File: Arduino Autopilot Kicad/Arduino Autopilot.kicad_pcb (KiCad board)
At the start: 2 copper layers, 100 x 77 mm, 28 parts, among them J1 12V_in, J2 to_clock, J3 to_RTC, J4 to_LCD, SW1 SW_Push

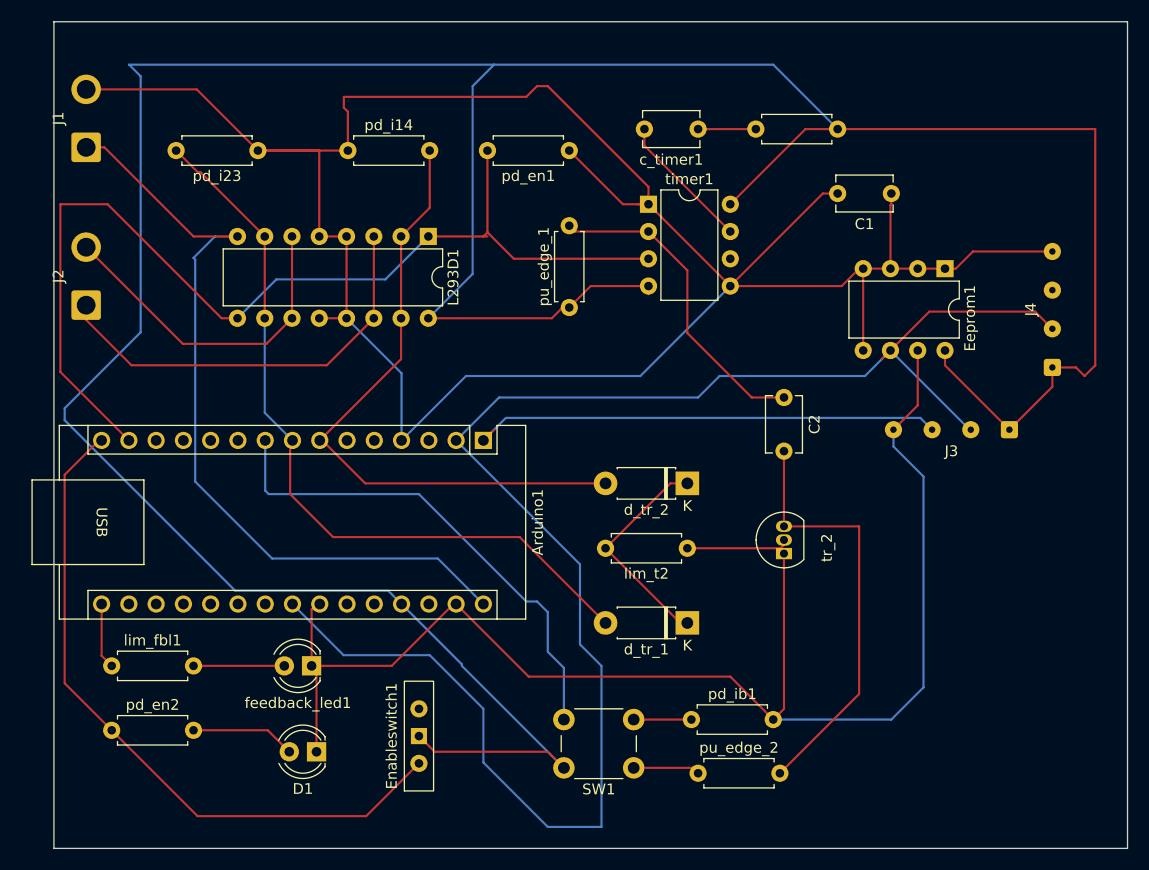
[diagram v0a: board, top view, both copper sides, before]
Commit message: updated board circuit, added serial commands parsing, update documentation
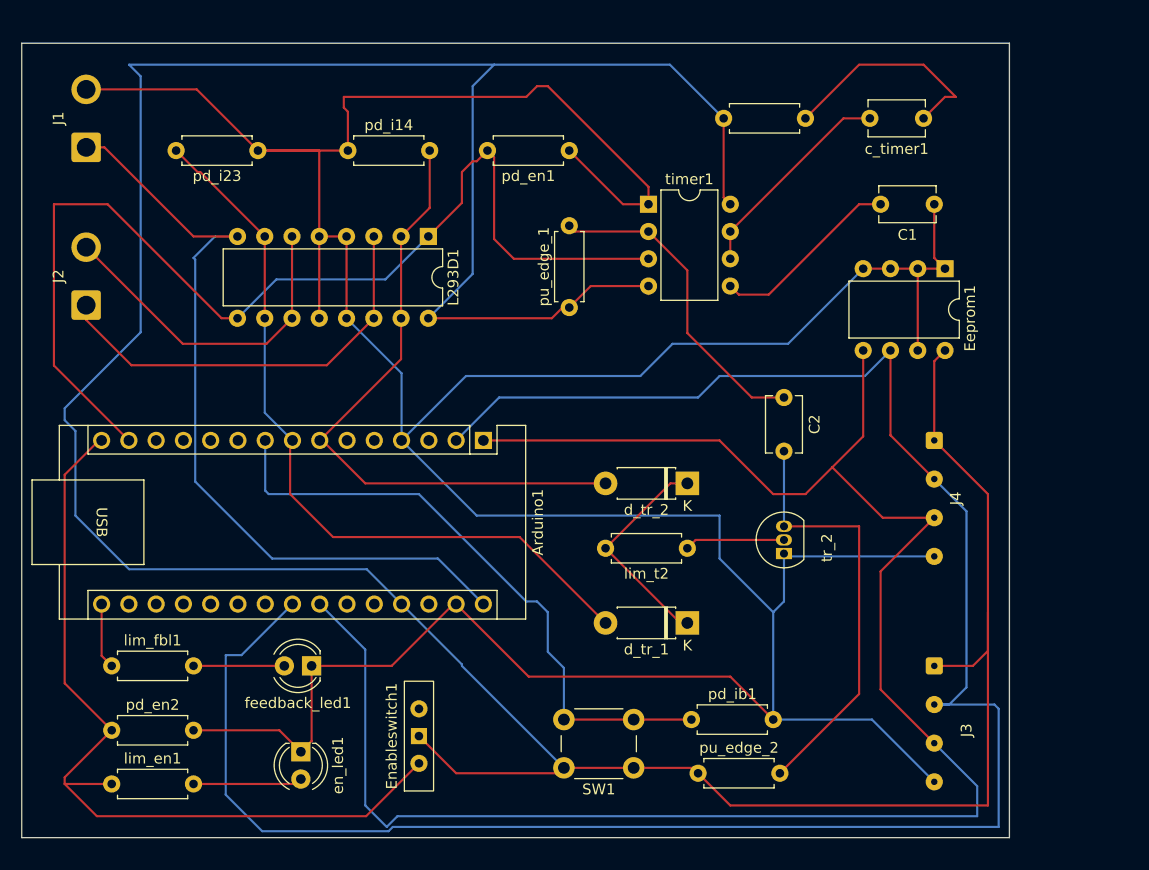
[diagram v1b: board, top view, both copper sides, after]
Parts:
- removed D1: LED, LED_THT:LED_D4.0mm
- added en_led1: LED, LED_THT:LED_D4.0mm, F.Cu at (55.0, 116.0)
- added lim_en1: R, Resistor_THT:R_Axial_DIN0207_L6.3mm_D2.5mm_P7.62mm_Horizontal, F.Cu at (37.4, 119.0)
- moved J3 23.1 mm to (114.0, 108.0), turned to -90 degrees
- moved c_timer1 21.0 mm to (113.0, 57.0)
- moved J4 12.9 mm to (114.0, 87.0), turned to -90 degrees
- moved r_timer1 4.73 mm to (102.0, 57.0), turned to 180 degrees
- moved C1 4.12 mm to (114.0, 65.0)
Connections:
- Arduino1 pad 1: Net-(Arduino1-D1/TX) -> Net-(Arduino1-A5)
- Arduino1 pad 24: GND -> Net-(Arduino1-A5)
- Eeprom1 pad 5: GND -> Net-(Arduino1-A5)
- J3 pad 3: Net-(Arduino1-D1/TX) -> Net-(Arduino1-A5)
- J4 pad 3: GND -> Net-(Arduino1-A5)
- pd_en2 pad 2: Net-(D1-A) -> GND
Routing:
- net Net-(Arduino1-A5): track 0.00 -> 171.5 mm
- net Net-(Arduino1-D1/TX): track 44.5 -> 0.00 mm
- net Net-(Arduino1-A4): track 154.8 -> 193.8 mm
- net Net-(c_timer1-Pad1): track 5.38 -> 21.1 mm
- net GND: track 340.4 -> 354.9 mm
- net Net-(Arduino1-D12): track 64.5 -> 78.0 mm
- net Net-(en_led1-A): track 0.00 -> 10.2 mm
- net +5V: track 315.5 -> 325.6 mm
- net Net-(D1-A): track 9.75 -> 0.00 mm
- net Net-(timer1-DIS): track 12.9 -> 19.9 mm
- net Net-(Arduino1-D6): track 51.7 -> 58.2 mm
- net Net-(Arduino1-D11): track 96.9 -> 102.2 mm
- net Net-(timer1-CV): track 13.0 -> 17.8 mm
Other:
- board size 100 x 77 mm -> 92 x 74 mm

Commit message: fixed dst management when sending manual inputs, fixed delay capacitor wiring in circuit
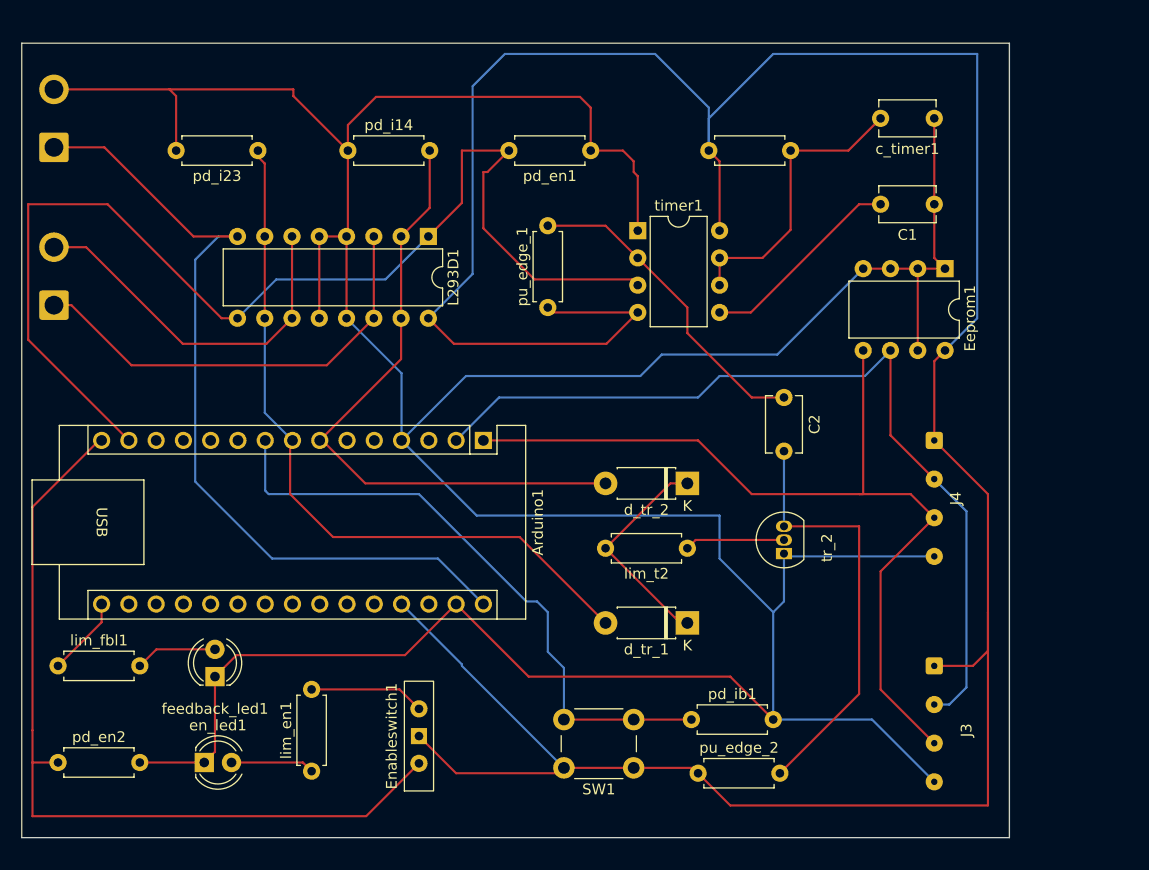
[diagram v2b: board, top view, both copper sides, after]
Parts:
- moved lim_en1 18.7 mm to (56.0, 117.8), turned to 90 degrees
- moved en_led1 9.06 mm to (46.0, 117.0), turned to 0 degrees
- moved feedback_led1 9.06 mm to (47.0, 109.0), turned to 90 degrees
- moved pd_en2 5.83 mm to (32.4, 117.0)
- moved lim_fbl1 5.00 mm to (32.4, 108.0)
- moved r_timer1 3.30 mm to (100.6, 60.0)
- moved J1 3.00 mm to (32.0, 59.7)
- moved J2 3.00 mm to (32.0, 74.4)
- moved timer1 2.66 mm to (86.4, 67.5)
- moved pd_en1 2.00 mm to (82.0, 60.0)
- moved pu_edge_1 2.00 mm to (78.0, 74.6)
- moved c_timer1 1.00 mm to (114.0, 57.0)
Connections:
- Arduino1 pad 1: Net-(Arduino1-A5) -> Net-(Arduino1-D1/TX)
- Arduino1 pad 2: Net-(Arduino1-A4) -> Net-(Arduino1-D0/RX)
- Arduino1 pad 23: Net-(Arduino1-A4) -> unconnected-(Arduino1-A4-Pad23)
- Arduino1 pad 24: Net-(Arduino1-A5) -> unconnected-(Arduino1-A5-Pad24)
- Eeprom1 pad 5: Net-(Arduino1-A5) -> Net-(Arduino1-D1/TX)
- Eeprom1 pad 6: Net-(Arduino1-A4) -> Net-(Arduino1-D0/RX)
- Enableswitch1 pad 3: unconnected-(Enableswitch1-A-Pad3) -> Net-(Enableswitch1-A)
- J3 pad 2: Net-(Arduino1-A4) -> Net-(Arduino1-D0/RX)
- J3 pad 3: Net-(Arduino1-A5) -> Net-(Arduino1-D1/TX)
- J4 pad 2: Net-(Arduino1-A4) -> Net-(Arduino1-D0/RX)
- J4 pad 3: Net-(Arduino1-A5) -> Net-(Arduino1-D1/TX)
- c_timer1 pad 1: Net-(c_timer1-Pad1) -> GND
- lim_en1 pad 1: Net-(Arduino1-D12) -> Net-(en_led1-A)
- lim_en1 pad 2: Net-(en_led1-A) -> Net-(Enableswitch1-A)
- pd_i23 pad 1: GND -> Net-(Arduino1-D5)
- pd_i23 pad 2: Net-(Arduino1-D5) -> GND
- r_timer1 pad 1: Net-(c_timer1-Pad1) -> Net-(timer1-DIS)
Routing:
- net Net-(Arduino1-A4): track 193.8 -> 0.00 mm
- net Net-(Arduino1-A5): track 171.5 -> 0.00 mm
- net Net-(Arduino1-D1/TX): track 0.00 -> 83.5 mm
- net Net-(Arduino1-D0/RX): track 0.00 -> 82.4 mm
- net +5V: track 325.6 -> 281.8 mm
- net Net-(c_timer1-Pad1): track 21.1 -> 0.00 mm
- net Net-(Enableswitch1-A): track 0.00 -> 10.7 mm
- net Net-(timer1-DIS): track 19.9 -> 27.2 mm
- net Net-(Arduino1-D11): track 102.2 -> 109.4 mm
- net GND: track 354.9 -> 361.4 mm
- net Net-(Arduino1-D5): track 71.3 -> 67.8 mm
- net Net-(J2-Pin_2): track 31.5 -> 34.5 mm
- net Net-(en_led1-A): track 10.2 -> 7.80 mm
- net Net-(J2-Pin_1): track 39.4 -> 41.5 mm
- net +12C: track 75.9 -> 77.6 mm
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
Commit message: updated pin layout, updated circuit and board design
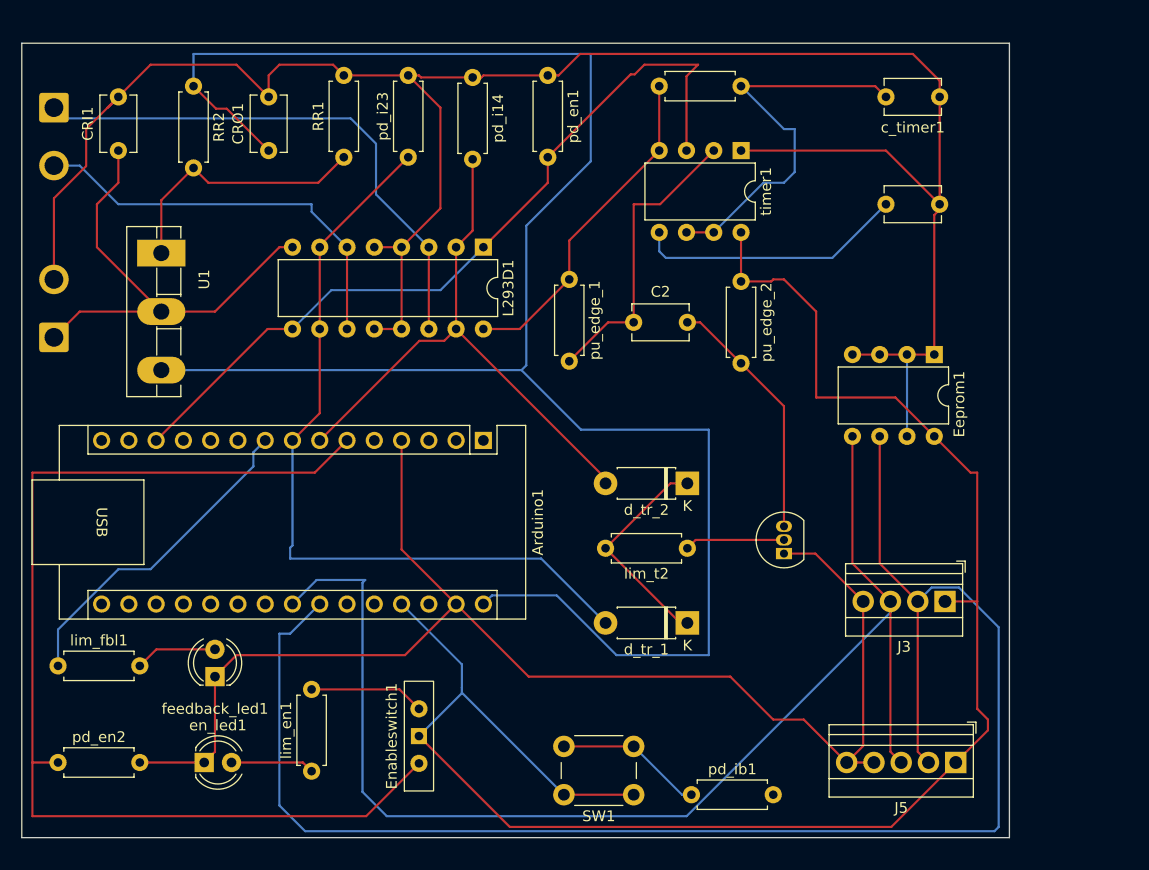
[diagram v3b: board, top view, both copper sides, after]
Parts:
- removed J4: to_LCD, Connector_Wire:SolderWire-0.1sqmm_1x04_P3.6mm_D0.4mm_OD1mm
- added CRI1: 0.1uf, Capacitor_THT:C_Disc_D5.1mm_W3.2mm_P5.00mm, F.Cu at (38.0, 60.0)
- added CRO1: 10uF, Capacitor_THT:C_Disc_D5.1mm_W3.2mm_P5.00mm, F.Cu at (52.0, 60.0)
- added J5: to_RTC, TerminalBlock:TerminalBlock_Xinya_XY308-2.54-5P_1x05_P2.54mm_Horizontal, F.Cu at (116.0, 117.0)
- added RR1: 1k, Resistor_THT:R_Axial_DIN0207_L6.3mm_D2.5mm_P7.62mm_Horizontal, F.Cu at (59.0, 60.6)
- added RR2: 330, Resistor_THT:R_Axial_DIN0207_L6.3mm_D2.5mm_P7.62mm_Horizontal, F.Cu at (45.0, 54.0)
- added U1: LM350_TO3, Package_TO_SOT_THT:TO-3PB-3_Vertical, F.Cu at (42.0, 69.5)
- J3: value to_RTC -> to_LCD; footprint Connector_Wire:SolderWire-0.1sqmm_1x04_P3.6mm_D0.4mm_OD1mm -> TerminalBlock:TerminalBlock_Xinya_XY308-2.54-4P_1x04_P2.54mm_Horizontal
- moved pu_edge_2 46.0 mm to (96.0, 72.2), turned to -90 degrees
- moved J2 18.4 mm to (32.0, 56.0), turned to -90 degrees
- moved J1 17.7 mm to (32.0, 77.4)
- moved C2 15.7 mm to (86.0, 76.0), turned to 0 degrees
- moved pd_i23 14.0 mm to (65.0, 60.6), turned to 90 degrees
- moved pd_i14 13.5 mm to (71.0, 53.2), turned to -90 degrees
- moved timer1 12.2 mm to (96.0, 60.0), turned to -90 degrees
- moved Eeprom1 8.06 mm to (114.0, 79.0)
- moved pd_en1 8.06 mm to (78.0, 53.0), turned to -90 degrees
- moved r_timer1 7.57 mm to (96.0, 54.0)
- moved pd_ib1 7.00 mm to (91.4, 120.0)
- moved J3 6.08 mm to (115.0, 102.0), turned to 180 degrees
- moved L293D1 5.22 mm to (72.0, 69.0)
- moved pu_edge_1 3.30 mm to (80.0, 72.0), turned to -90 degrees
- moved SW1 2.50 mm to (86.0, 120.0)
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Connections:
- Arduino1 pad 1: Net-(Arduino1-D1/TX) -> unconnected-(Arduino1-D1/TX-Pad1)
- Arduino1 pad 13: unconnected-(Arduino1-D10-Pad13) -> Net-(Arduino1-D10)
- Arduino1 pad 14: Net-(Arduino1-D11) -> unconnected-(Arduino1-D11-Pad14)
- Arduino1 pad 15: Net-(Arduino1-D12) -> unconnected-(Arduino1-D12-Pad15)
- Arduino1 pad 16: Net-(Arduino1-D13) -> unconnected-(Arduino1-D13-Pad16)
- Arduino1 pad 2: Net-(Arduino1-D0/RX) -> unconnected-(Arduino1-D0/RX-Pad2)
- Arduino1 pad 23: unconnected-(Arduino1-A4-Pad23) -> Net-(Arduino1-A4)
- Arduino1 pad 24: unconnected-(Arduino1-A5-Pad24) -> Net-(Arduino1-A5)
- Arduino1 pad 30: +12C -> Net-(Arduino1-VIN)
- Arduino1 pad 6: unconnected-(Arduino1-D3-Pad6) -> Net-(Arduino1-D3)
- Eeprom1 pad 5: Net-(Arduino1-D1/TX) -> Net-(Arduino1-A4)
- Eeprom1 pad 6: Net-(Arduino1-D0/RX) -> Net-(Arduino1-A5)
- Enableswitch1 pad 2: Net-(Arduino1-D12) -> Net-(Arduino1-D3)
- J3 pad 2: Net-(Arduino1-D0/RX) -> Net-(Arduino1-A5)
- J3 pad 3: Net-(Arduino1-D1/TX) -> Net-(Arduino1-A4)
- L293D1 pad 1: Net-(Arduino1-D11) -> Net-(Arduino1-D10)
- L293D1 pad 9: Net-(Arduino1-D11) -> Net-(Arduino1-D10)
- SW1 pad 2: Net-(Arduino1-D6) -> Net-(SW1-Pad2)
- lim_fbl1 pad 1: Net-(Arduino1-D13) -> Net-(Arduino1-D6)
- pd_en1 pad 2: Net-(Arduino1-D11) -> Net-(Arduino1-D10)
- pd_en2 pad 1: Net-(Arduino1-D12) -> Net-(Arduino1-D3)
- pd_ib1 pad 1: Net-(Arduino1-D6) -> Net-(SW1-Pad2)
- timer1 pad 3: Net-(Arduino1-D11) -> Net-(Arduino1-D10)
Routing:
- net Net-(Arduino1-VIN): track 0.00 -> 180.1 mm
- net Net-(Arduino1-A5): track 0.00 -> 149.5 mm
- net Net-(Arduino1-A4): track 0.00 -> 118.8 mm
- net Net-(Arduino1-D11): track 109.4 -> 0.00 mm
- net Net-(Arduino1-D3): track 0.00 -> 103.0 mm
- net +5V: track 281.8 -> 194.5 mm
- net Net-(Arduino1-D1/TX): track 83.5 -> 0.00 mm
- net Net-(Arduino1-D0/RX): track 82.4 -> 0.00 mm
- net Net-(Arduino1-D12): track 78.3 -> 0.00 mm
- net Net-(Arduino1-D10): track 0.00 -> 74.8 mm
- net GND: track 361.4 -> 326.4 mm
- net +12C: track 77.6 -> 44.0 mm
- net Net-(Arduino1-D6): track 58.2 -> 30.8 mm
- net Net-(U1-ADJ): track 0.00 -> 24.7 mm
- net Net-(tr_2-C): track 40.1 -> 23.4 mm
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
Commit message: fixed sleep mode, updated diagrams
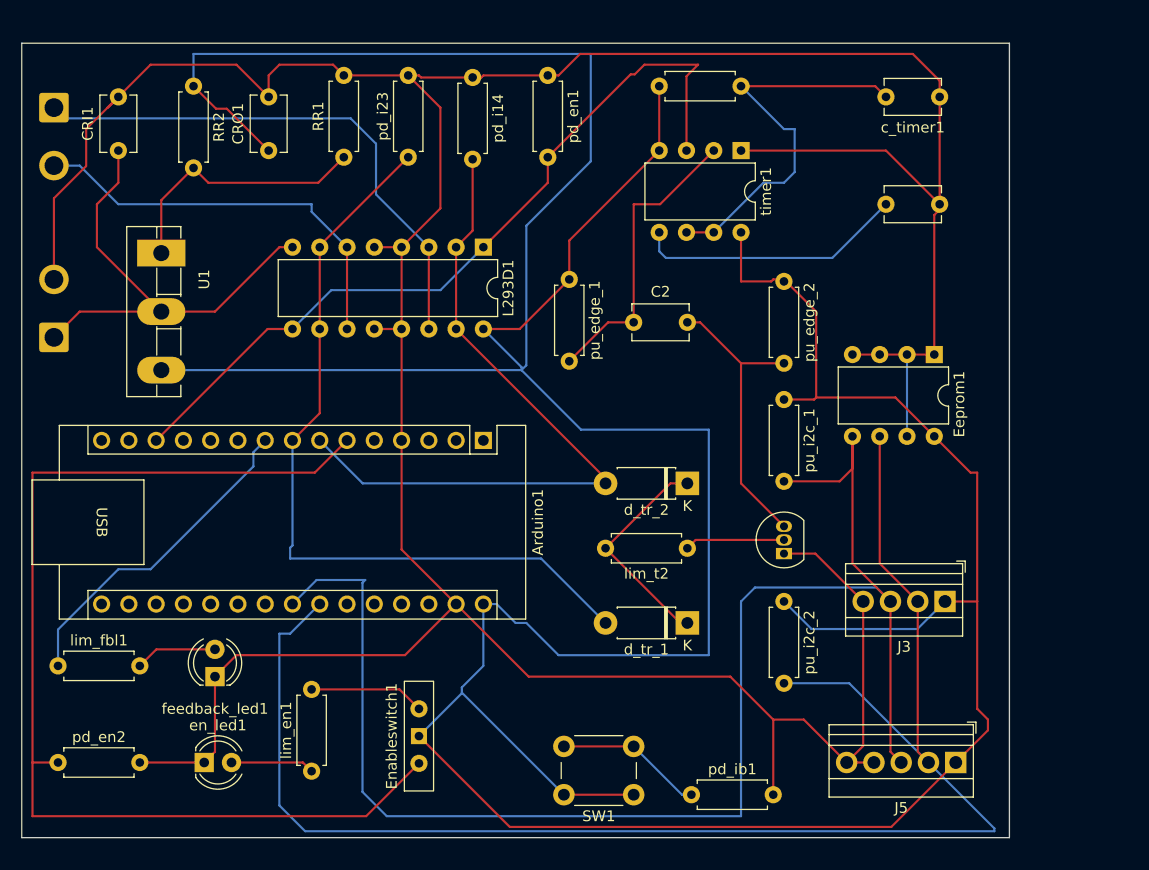
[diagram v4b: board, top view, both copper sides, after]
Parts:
- added pu_i2c_1: R, Resistor_THT:R_Axial_DIN0207_L6.3mm_D2.5mm_P7.62mm_Horizontal, F.Cu at (100.0, 83.2)
- added pu_i2c_2: R, Resistor_THT:R_Axial_DIN0207_L6.3mm_D2.5mm_P7.62mm_Horizontal, F.Cu at (100.0, 102.0)
- moved pu_edge_2 4.00 mm to (100.0, 72.2)
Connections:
- Arduino1 pad 27: +5V -> unconnected-(Arduino1-+5V-Pad27)
- Arduino1 pad 30: Net-(Arduino1-VIN) -> +5V
- CRO1 pad 1: Net-(Arduino1-VIN) -> +5V
- RR2 pad 1: Net-(Arduino1-VIN) -> +5V
- U1 pad 3: Net-(Arduino1-VIN) -> +5V
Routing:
- net +5V: track 194.5 -> 398.4 mm
- net Net-(Arduino1-VIN): track 180.1 -> 0.00 mm
- net Net-(Arduino1-A4): track 118.8 -> 140.9 mm
- net GND: track 326.4 -> 343.8 mm
- net Net-(Arduino1-D4): track 53.6 -> 64.9 mm
- net Net-(tr_2-C): track 23.4 -> 27.4 mm
- net Net-(Arduino1-A5): track 149.5 -> 146.2 mm
